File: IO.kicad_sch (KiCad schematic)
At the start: 18 parts, among them J5 Conn_01x14_Pin, J8 Conn_01x14_Pin, J9 Conn_01x04_Pin, Q2 BSS84, SW1 SW_Push

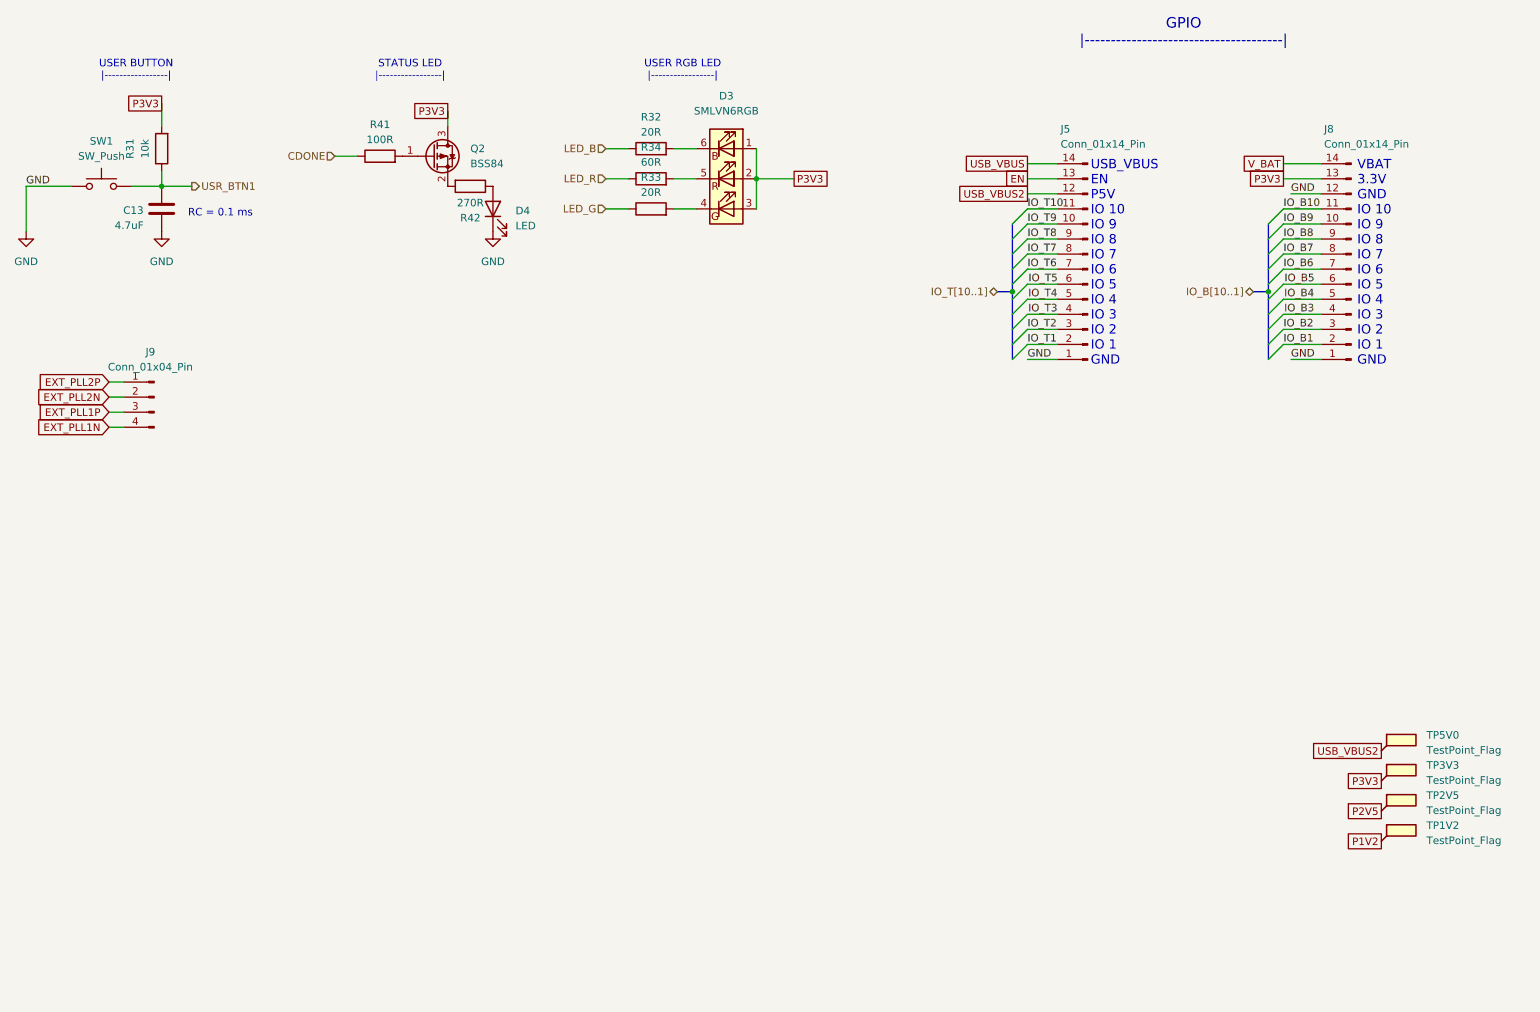
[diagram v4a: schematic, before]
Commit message: End of Version 1.0. Feedback received
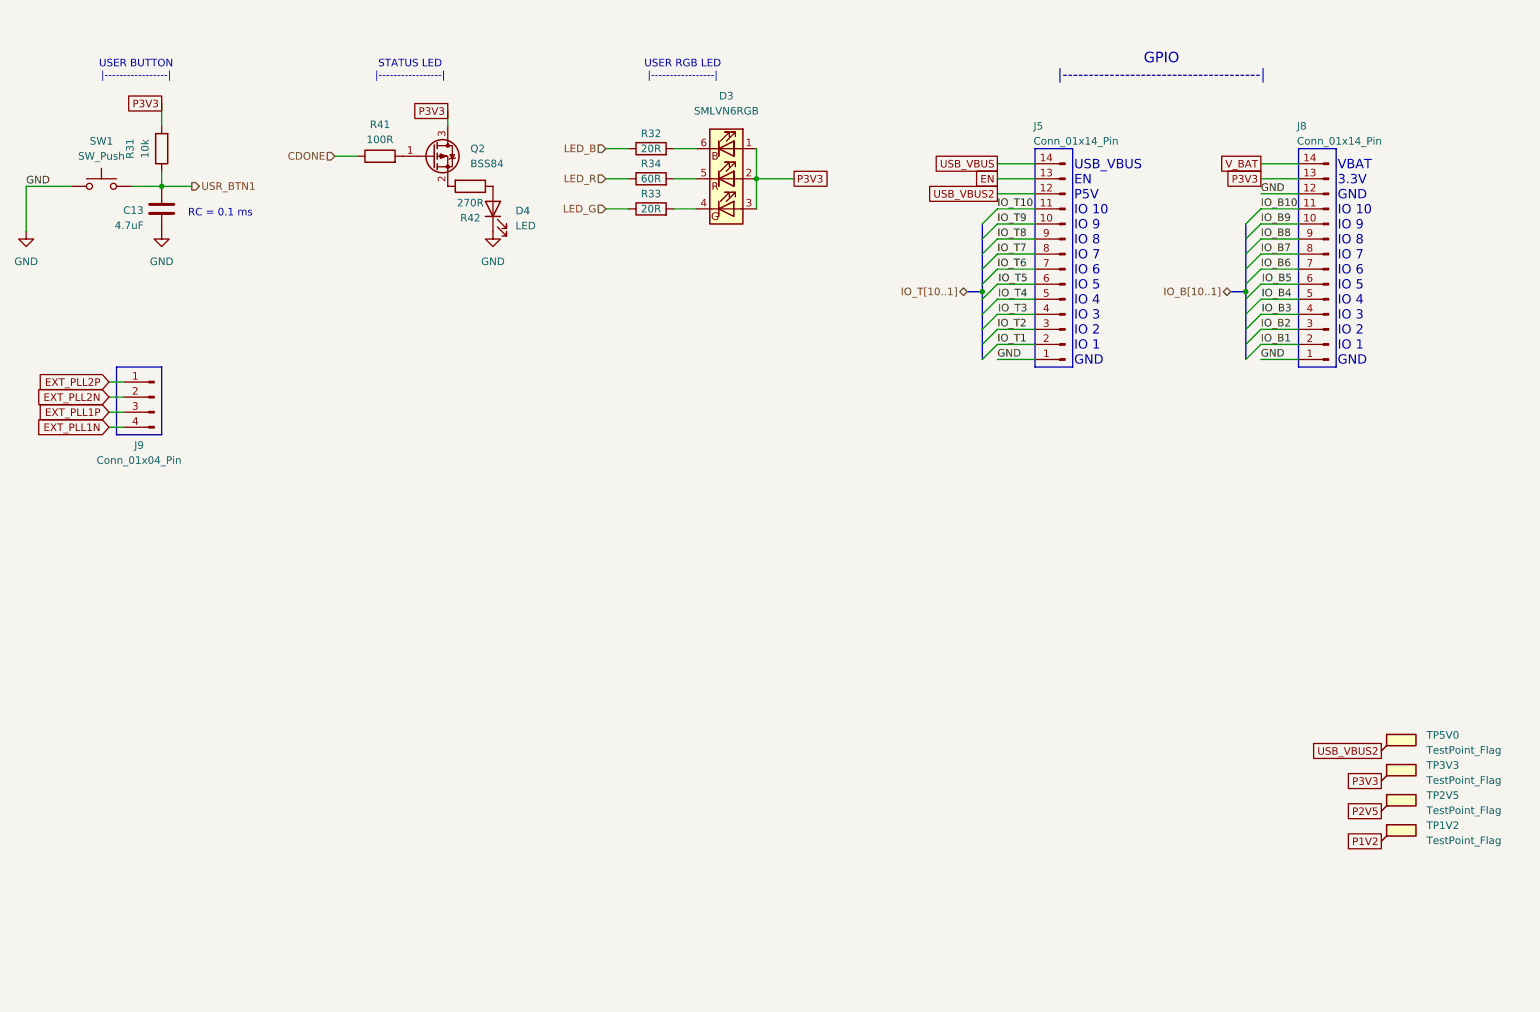
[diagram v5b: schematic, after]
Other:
- moved on the sheet: J5, J8
